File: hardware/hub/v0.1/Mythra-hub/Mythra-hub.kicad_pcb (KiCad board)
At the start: 4 copper layers, 65 x 68 mm, 21 parts, among them J1 USB_C_Receptacle, U1 TUSB8042A, U2 HD3SS460, Y1 24MHz

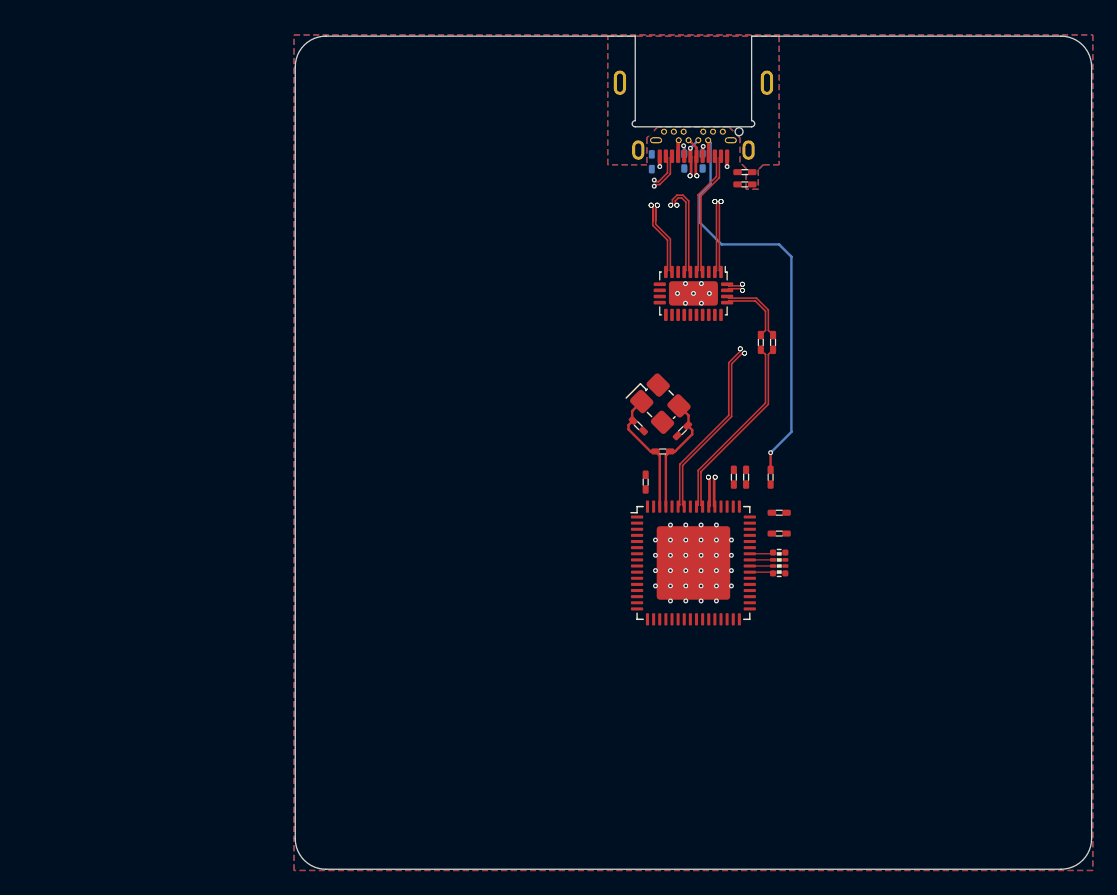
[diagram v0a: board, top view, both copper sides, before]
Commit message: Fixed up the stackup for the PCB and cleaned up after the change
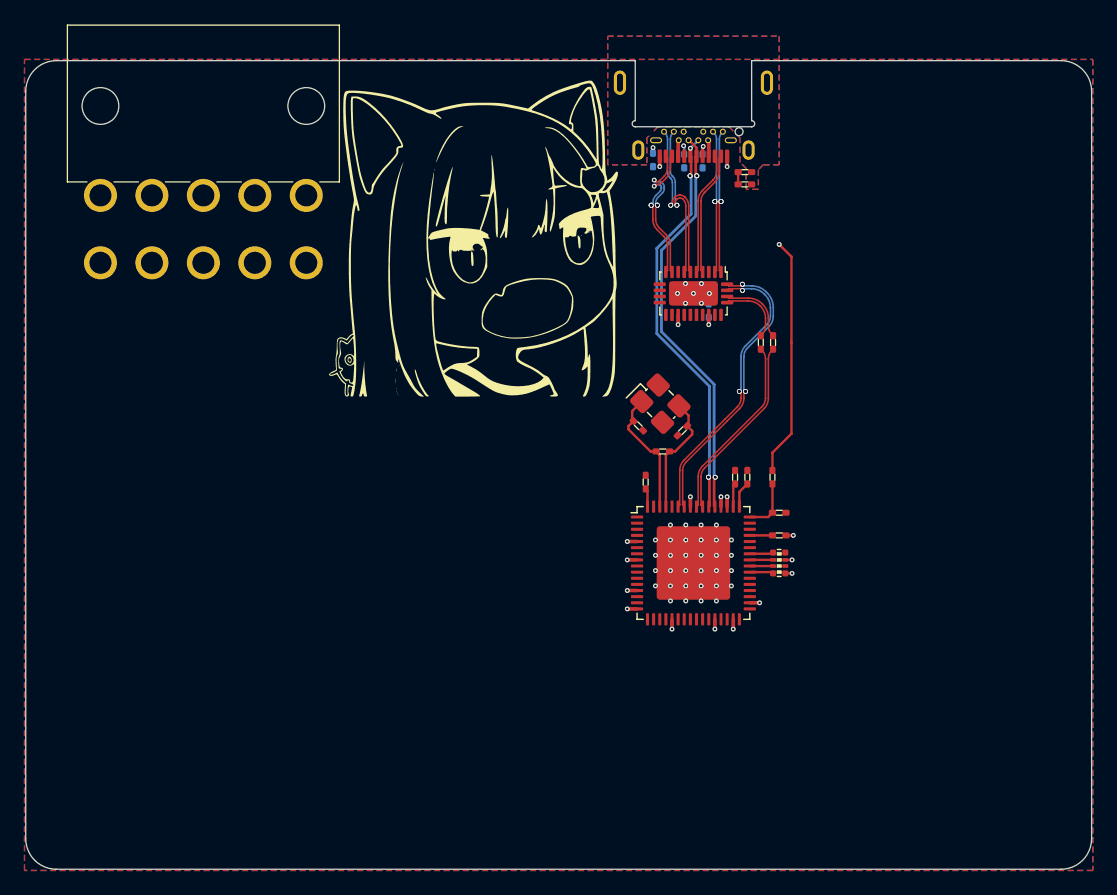
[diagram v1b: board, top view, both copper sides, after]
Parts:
- added C8: 0.1uF, rhais_rcl:C0402, B.Cu at (151.2, 79.4)
- added G***: nya_a, lethalbit-graphics:nya_a, F.Cu at (132.7, 73.3)
- added J2: Molex Power Input, rhais_connector-molex:39-30-1101, F.Cu at (110.0, 70.0)
- J1: value USB_C_Receptacle -> 918-418K2022C40000
- moved C5 0.18 mm to (146.7, 67.1)
- moved R10 0.15 mm to (157.0, 97.8)
- moved R5 0.15 mm to (156.4, 93.0)
- moved C4 0.10 mm to (153.4, 93.0)
- moved R3 0.10 mm to (154.4, 93.0)
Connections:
- U1 pad 1: unconnected-(U1-Pad1) -> /DFP1/DFP_D+
- U1 pad 10: unconnected-(U1-Pad10) -> /DFP2/DFP_D-
- U1 pad 11: unconnected-(U1-Pad11) -> /DFP2/DFP_TX+
- U1 pad 12: unconnected-(U1-Pad12) -> /DFP2/DFP_TX-
- U1 pad 14: unconnected-(U1-Pad14) -> /DFP2/DFP_RX+
- U1 pad 15: unconnected-(U1-Pad15) -> /DFP2/DFP_RX-
- U1 pad 17: unconnected-(U1-Pad17) -> /DFP3/DFP_D+
- U1 pad 18: unconnected-(U1-Pad18) -> /DFP3/DFP_D-
- U1 pad 19: unconnected-(U1-Pad19) -> /DFP3/DFP_TX+
- U1 pad 2: unconnected-(U1-Pad2) -> /DFP1/DFP_D-
- U1 pad 20: unconnected-(U1-Pad20) -> /DFP3/DFP_TX-
- U1 pad 22: unconnected-(U1-Pad22) -> /DFP3/DFP_RX+
- U1 pad 23: unconnected-(U1-Pad23) -> /DFP3/DFP_RX-
- U1 pad 24: unconnected-(U1-Pad24) -> /DFP4/DFP_D+
- U1 pad 25: unconnected-(U1-Pad25) -> /DFP4/DFP_D-
- U1 pad 26: unconnected-(U1-Pad26) -> /DFP4/DFP_TX+
- U1 pad 27: unconnected-(U1-Pad27) -> /DFP4/DFP_TX-
- U1 pad 29: unconnected-(U1-Pad29) -> /DFP4/DFP_RX+
- U1 pad 3: unconnected-(U1-Pad3) -> /DFP1/DFP_TX+
- U1 pad 30: unconnected-(U1-Pad30) -> /DFP4/DFP_RX-
- U1 pad 32: unconnected-(U1-Pad32) -> /PWR4
- U1 pad 33: unconnected-(U1-Pad33) -> /PWR3
- U1 pad 35: unconnected-(U1-Pad35) -> /PWR2
- U1 pad 36: unconnected-(U1-Pad36) -> /PWR1
- U1 pad 4: unconnected-(U1-Pad4) -> /DFP1/DFP_TX-
- U1 pad 43: unconnected-(U1-Pad43) -> /OC4
- U1 pad 44: unconnected-(U1-Pad44) -> /OC3
- U1 pad 46: unconnected-(U1-Pad46) -> /OC1
- U1 pad 47: unconnected-(U1-Pad47) -> /OC2
- U1 pad 6: unconnected-(U1-Pad6) -> /DFP1/DFP_RX+
- U1 pad 7: unconnected-(U1-Pad7) -> /DFP1/DFP_RX-
- U1 pad 9: unconnected-(U1-Pad9) -> /DFP2/DFP_D+
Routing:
- net +1V1: track 0.00 -> 6.40 mm, vias 0 -> 8
- net +3V3: track 0.00 -> 5.70 mm, vias 0 -> 8
- net /UFP/UP_VBUS: track 0.00 -> 4.34 mm
- net Net-(R3-Pad1): track 0.00 -> 2.12 mm
- net Net-(C4-Pad1): track 0.00 -> 1.91 mm
- net Net-(R10-Pad1): track 0.00 -> 1.85 mm
- net Net-(R2-Pad1): track 0.00 -> 1.51 mm
- net /UFP/UP_RX2-: track 13.0 -> 11.6 mm
- net /UFP/UP_RX2+: track 13.0 -> 11.6 mm
- net +12V: track 0.00 -> 1.41 mm
- net GND: track 1.70 -> 2.70 mm
- net /UFP/UP_RX+: track 24.7 -> 24.4 mm, vias 4 -> 5
- net /UFP/UP_RX-: track 24.4 -> 24.0 mm, vias 4 -> 5
- net +5V: vias 1 -> 2
- added copper zone on In2.Cu, net +12V
- added copper zone on In2.Cu, net +1V1
- added copper zone on In3.Cu, net /UFP/UP_SHIELD
- added copper zone on In4.Cu, net /UFP/UP_SHIELD
- added copper zone on In2.Cu, net GND
- added copper zone on In3.Cu, net GND
- added copper zone on In4.Cu, net GND
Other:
- board size 65 x 68 mm -> 87 x 66 mm
- copper layers 4 -> 6
- board text added: "BOT"
- board text added: "Board Stackup"
- board text added: "Core"
- board text added: "GND"
- board text added: "Mixed"
- board text added: "PWR"
- board text added: "Pre-Preg"
- board text added: "SIG"
- board text added: "TOP"

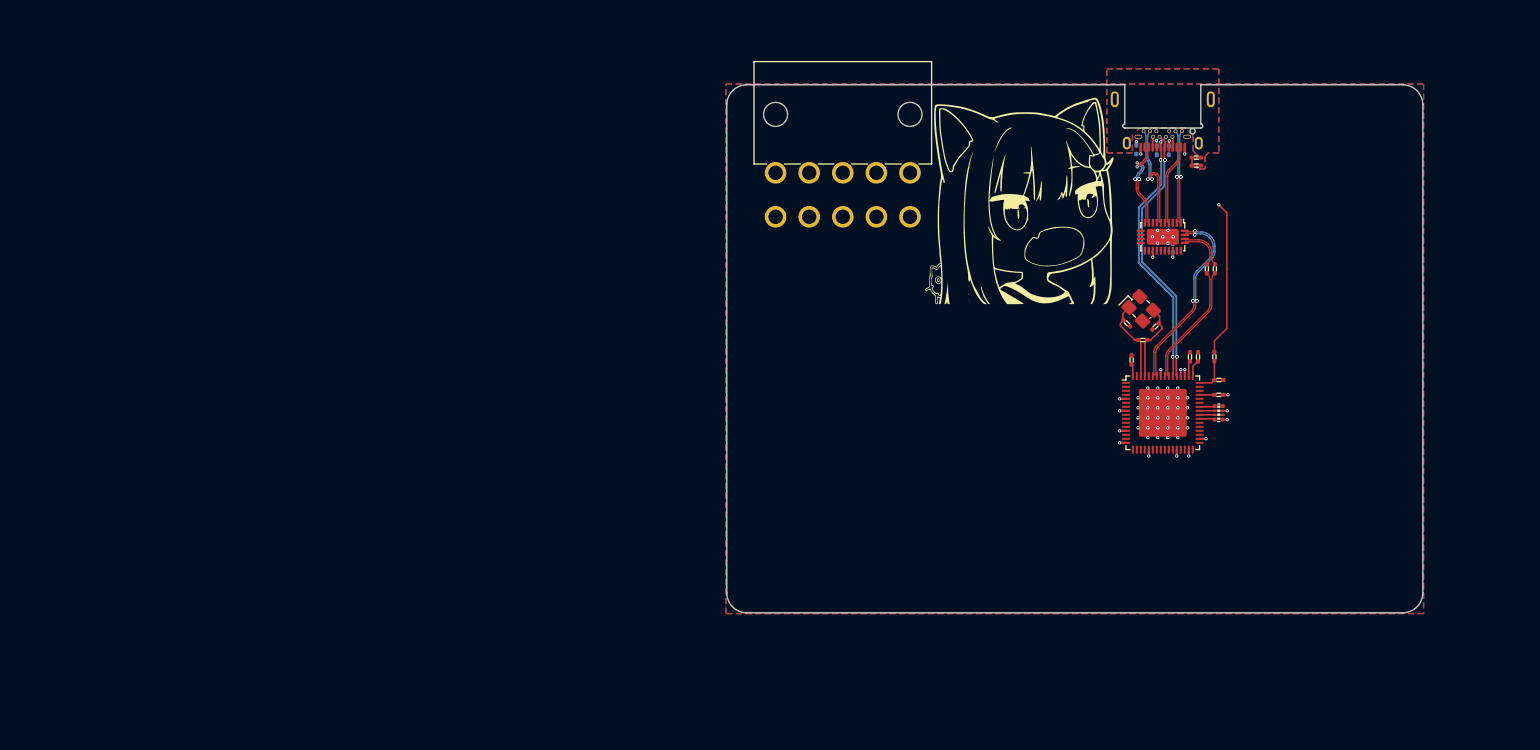
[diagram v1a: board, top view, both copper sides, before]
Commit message: Placed and routed the new DC-DC power supply and the DFP connectors
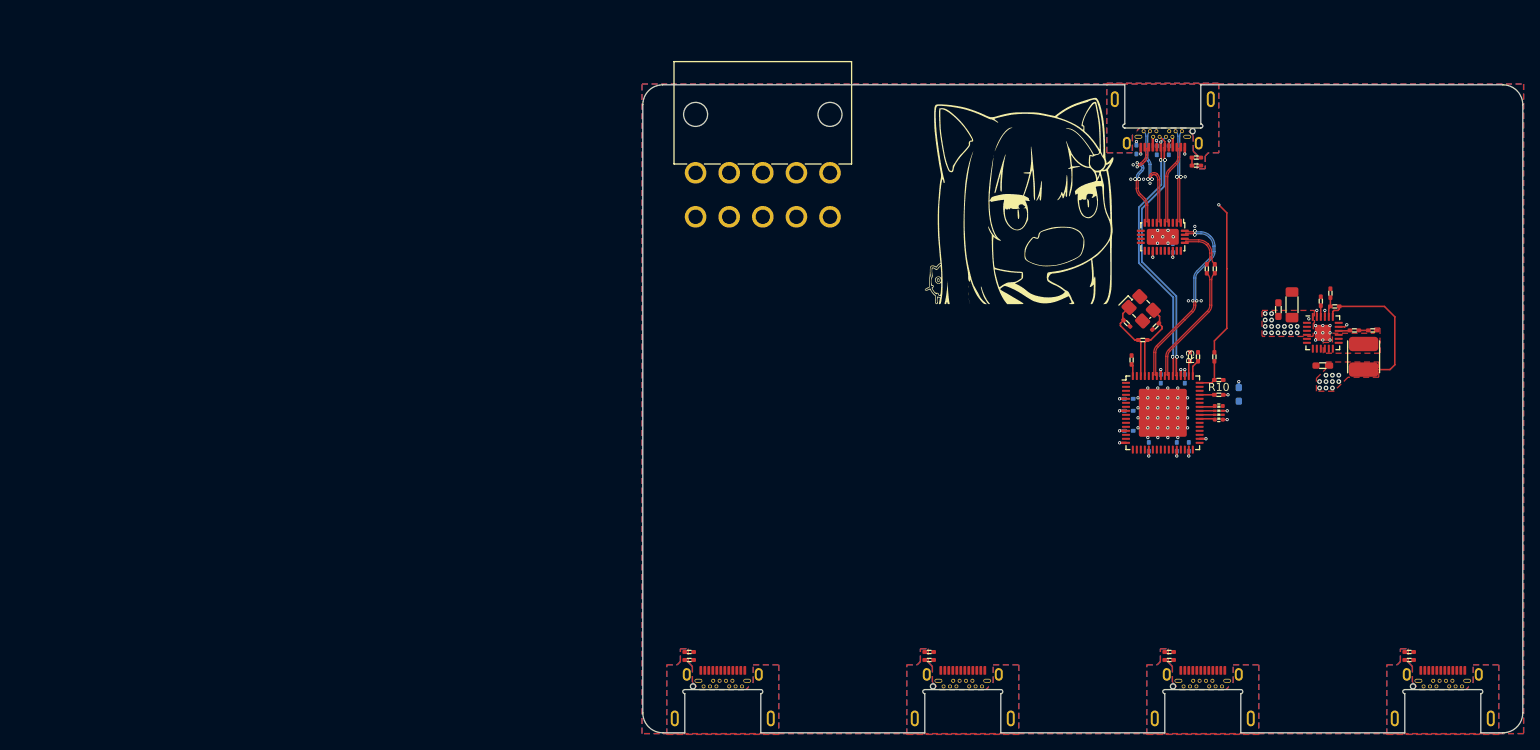
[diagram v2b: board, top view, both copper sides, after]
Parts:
- added C10: 0.1uF, rhais_rcl:C0402, B.Cu at (151.8, 104.2)
- added C11: 0.1uF, rhais_rcl:C0402, B.Cu at (153.2, 104.2)
- added C12: 0.1uF, rhais_rcl:C0402, B.Cu at (145.8, 102.2)
- added C13: 0.1uF, rhais_rcl:C0402, B.Cu at (145.8, 99.8)
- added C14: 0.1uF, rhais_rcl:C0402, B.Cu at (145.8, 98.2)
- added C15: 0.1uF, rhais_rcl:C0402, B.Cu at (149.8, 95.8)
- added C16: 0.1uF, rhais_rcl:C0402, B.Cu at (152.8, 95.8)
- added C17: 10uF, rhais_rcl:C0603, B.Cu at (159.5, 97.7)
- added C18: 10uF, rhais_rcl:C0603, F.Cu at (164.4, 87.1)
- added C19: 22uF, rhais_rcl:C1206, F.Cu at (166.2, 86.5)
- added C20: 22uF, rhais_rcl:C0603, F.Cu at (170.0, 94.1)
- added C21: 4.7uF, rhais_rcl:C0402, F.Cu at (169.8, 86.0)
- added C22: 0.1uF, rhais_rcl:C0402, F.Cu at (176.2, 89.7)
- added C23: 0.1uF, rhais_rcl:C0402, F.Cu at (90.8, 129.9)
- added C24: 0.1uF, rhais_rcl:C0402, F.Cu at (120.8, 129.9)
- added C25: 0.1uF, rhais_rcl:C0402, F.Cu at (150.8, 129.9)
- added C26: 0.1uF, rhais_rcl:C0402, F.Cu at (180.8, 129.9)
- added C9: 0.1uF, rhais_rcl:C0402, B.Cu at (148.2, 104.2)
- added J3: 918-418K2022C40000, rhais_usb:USB-3.1-Type-C_In-PCB, F.Cu at (95.0, 134.6)
- added J4: 918-418K2022C40000, rhais_usb:USB-3.1-Type-C_In-PCB, F.Cu at (125.0, 134.6)
- added J5: 918-418K2022C40000, rhais_usb:USB-3.1-Type-C_In-PCB, F.Cu at (155.0, 134.6)
- added J6: 918-418K2022C40000, rhais_usb:USB-3.1-Type-C_In-PCB, F.Cu at (185.0, 134.6)
- added L1: 3.3uH, rhais_coilcraft:XAL40xx, F.Cu at (175.1, 93.0)
- added R11: 3.4k, rhais_rcl:R0402, F.Cu at (171.5, 86.7)
- added R12: 10k, rhais_rcl:R0402, F.Cu at (170.9, 85.0)
- added R13: 20R, rhais_rcl:R0402, F.Cu at (173.9, 89.7)
- added R14: 1M, rhais_rcl:R0402, F.Cu at (90.8, 130.9)
- added R15: 1M, rhais_rcl:R0402, F.Cu at (120.8, 130.9)
- added R16: 1M, rhais_rcl:R0402, F.Cu at (150.8, 130.9)
- added R17: 1M, rhais_rcl:R0402, F.Cu at (180.8, 130.9)
- added U3: BD95861MUV, rhais_package-qfn:VQFN-24-1EP_4x4mm_P0.5mm_EP2x2mm, F.Cu at (170.0, 90.0)
- R10, R3: footprint rhais_rcl:C0402 -> rhais_rcl:R0402
- moved J2 10.0 mm to (100.0, 70.0)
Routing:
- net +1V1: track 6.40 -> 31.5 mm, vias 8 -> 19
- net +12V: track 1.41 -> 7.59 mm, vias 0 -> 18
- net Net-(R11-Pad1): track 0.00 -> 2.50 mm
- net GND: track 2.70 -> 4.33 mm, vias 41 -> 61
- net Net-(R13-Pad1): track 0.00 -> 1.43 mm
- net Net-(C21-Pad1): track 0.00 -> 1.41 mm
- net Net-(C22-Pad1): track 0.00 -> 1.20 mm
- net /UFP/UP_RX-: vias 5 -> 3
- net /UFP/UP_RX+: vias 5 -> 3
- added copper zone on F.Cu, net +12V
- added copper zone on F.Cu, net +1V1
- added copper zone on B.Cu, net /DFP1/DN_SHIELD
- added copper zone on F.Cu, net /DFP1/DN_SHIELD
- added copper zone on In1.Cu, net /DFP1/DN_SHIELD
- added copper zone on In2.Cu, net /DFP1/DN_SHIELD
- added copper zone on In3.Cu, net /DFP1/DN_SHIELD
- added copper zone on In4.Cu, net /DFP1/DN_SHIELD
- added copper zone on B.Cu, net /DFP2/DN_SHIELD
- added copper zone on F.Cu, net /DFP2/DN_SHIELD
- added copper zone on In1.Cu, net /DFP2/DN_SHIELD
- added copper zone on In2.Cu, net /DFP2/DN_SHIELD
- added copper zone on In3.Cu, net /DFP2/DN_SHIELD
- added copper zone on In4.Cu, net /DFP2/DN_SHIELD
- added copper zone on B.Cu, net /DFP3/DN_SHIELD
- added copper zone on F.Cu, net /DFP3/DN_SHIELD
- added copper zone on In1.Cu, net /DFP3/DN_SHIELD
- added copper zone on In2.Cu, net /DFP3/DN_SHIELD
- added copper zone on In3.Cu, net /DFP3/DN_SHIELD
- added copper zone on In4.Cu, net /DFP3/DN_SHIELD
- added copper zone on B.Cu, net /DFP4/DN_SHIELD
- added copper zone on F.Cu, net /DFP4/DN_SHIELD
- added copper zone on In1.Cu, net /DFP4/DN_SHIELD
- added copper zone on In2.Cu, net /DFP4/DN_SHIELD
- added copper zone on In3.Cu, net /DFP4/DN_SHIELD
- added copper zone on In4.Cu, net /DFP4/DN_SHIELD
- added copper zone on F.Cu, net Net-(C22-Pad2)
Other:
- board size 87 x 66 mm -> 110 x 81 mm
